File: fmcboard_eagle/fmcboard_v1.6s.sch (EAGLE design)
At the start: 300 parts, among them IC1 OPA699ID, IC10 LM358, IC11 7805DT, IC12 SN74AUC2G66DCTR, IC13 SN74AUC2G66DCTR, IC14 SN74AUC2G66DCTR, IC15 SN74AUC2G66DCTR, IC16 DAC7578SPWR, IC17 SN74AUC2G66DCTR, IC18 SN74AUC2G66DCTR, IC19 SN74AUC2G66DCTR, IC2 DAC7578SPWR, IC20 SN74AUC2G66DCTR, IC21 74AUP2GU04GW, IC22 74AUP2GU04GW, IC23 74AUP2GU04GW, IC24 74AUP2GU04GW, IC25 MC7905ACD2TR4G, IC26 AMS1117-1.8, IC27 LM358, IC28 SN74AUC2G66DCTR, IC29 LM337KVURG3, IC3 LTC6229IMS8E#TRPBF, IC30 SN74AUC2G66DCTR, IC31 SN74AUC2G66DCTR, IC32 SN74AUC2G66DCTR, IC33 LTC6229IMS8E#TRPBF, IC34 74AUP2GU04GW, IC35 74AUP2GU04GW, IC36 TPS5430DDAR, IC37 TPS5430DDAR, IC4 OPA695IDR, IC5 LTC6229IMS8E#TRPBF, IC6 OPA695IDR, IC7 OPA699ID, IC8 LM358, IC9 LM358, J1 8pin, J12 4p-2.54, J13 4p-2.54, J2 ASP-134604-01, J3 2p-2.54, J4 4p-2.54, J5 4p-2.54, J8 4p-2.54, J9 2p-2.54

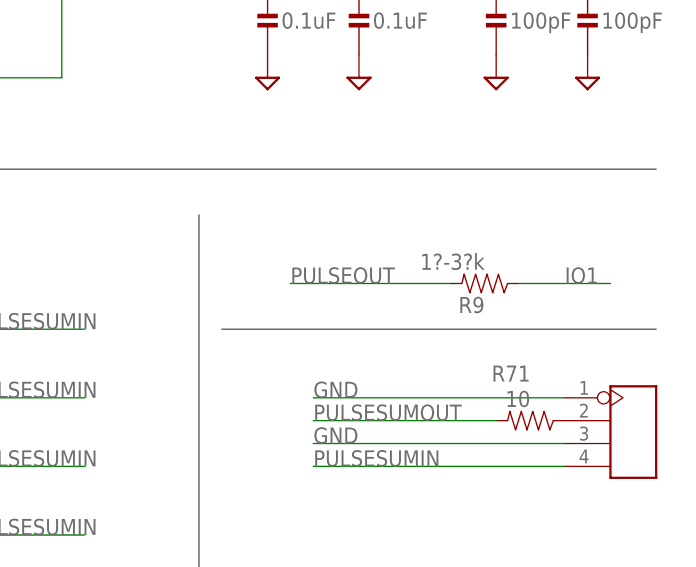
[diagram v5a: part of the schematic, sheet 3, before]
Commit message: v1.652s 0805 test resistor instead of 0402
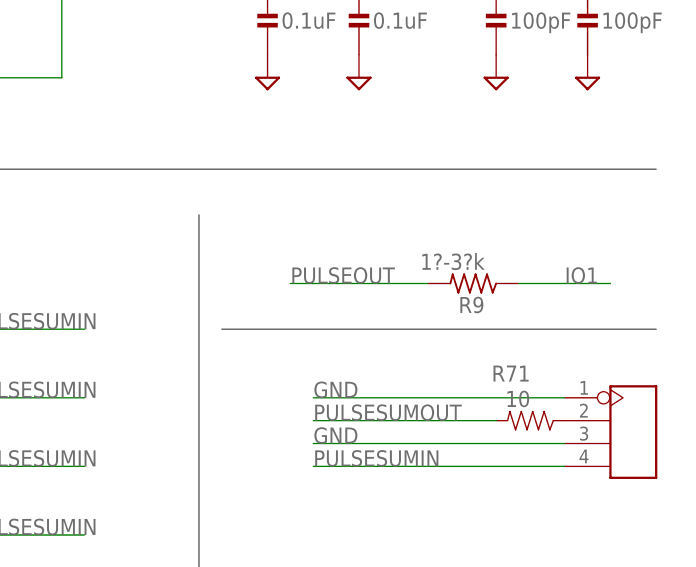
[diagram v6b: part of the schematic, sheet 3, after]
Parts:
- R9: device passives:RESISTOR0402_RES -> rcl:R-US_R0805
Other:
- moved on the sheet: R9
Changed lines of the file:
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@@
 <part name="SUPPLY125" library="supply2" library_urn="urn:adsk.eagle:library:372" deviceset="GND" device=""/>
 <part name="IC1" library="OPA699ID" deviceset="OPA699ID" device=""/>
-<part name="R9" library="passives" deviceset="RESISTOR" device="0402_RES" value="1?-3?k"/>
+<part name="R9" library="rcl" library_urn="urn:adsk.eagle:library:334" deviceset="R-US_" device="R0805" package3d_urn="urn:adsk.eagle:package:23553/2" value="1?-3?k"/>
 <part name="R10" library="passives" deviceset="RESISTOR" device="0402_RES" value="100"/>
 <part name="SUPPLY1" library="supply2" library_urn="urn:adsk.eagle:library:372" deviceset="GND" device=""/>
@@
 <segment>
 <pinref part="R9" gate="G$1" pin="2"/>
-<wire x1="269.24" y1="48.26" x2="251.46" y2="48.26" width="0.1524" layer="91"/>
+<wire x1="266.7" y1="48.26" x2="251.46" y2="48.26" width="0.1524" layer="91"/>
 <label x="251.46" y="48.26" size="1.778" layer="95"/>
 </segment>

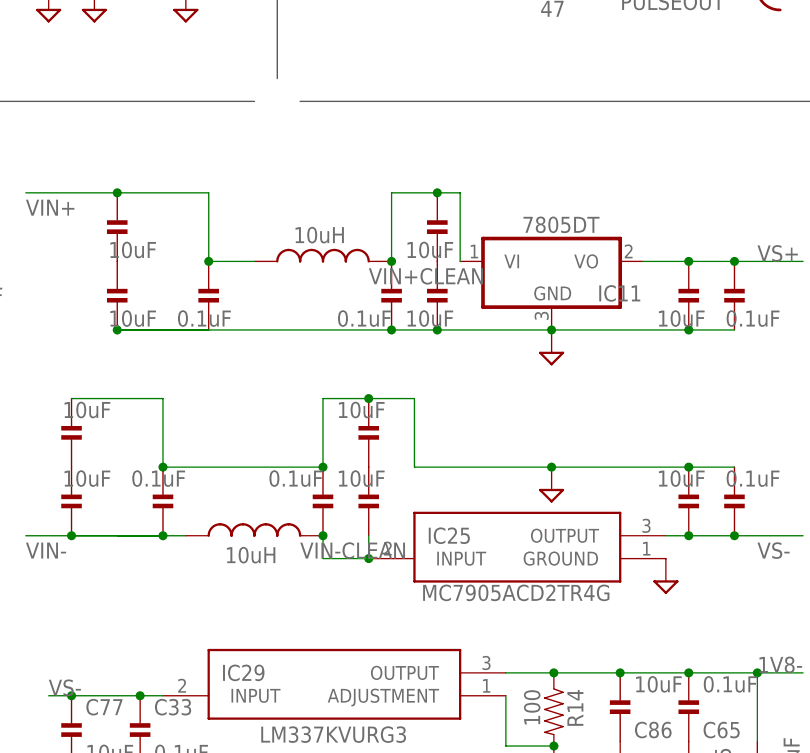
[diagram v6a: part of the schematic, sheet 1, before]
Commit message: fix VIN-
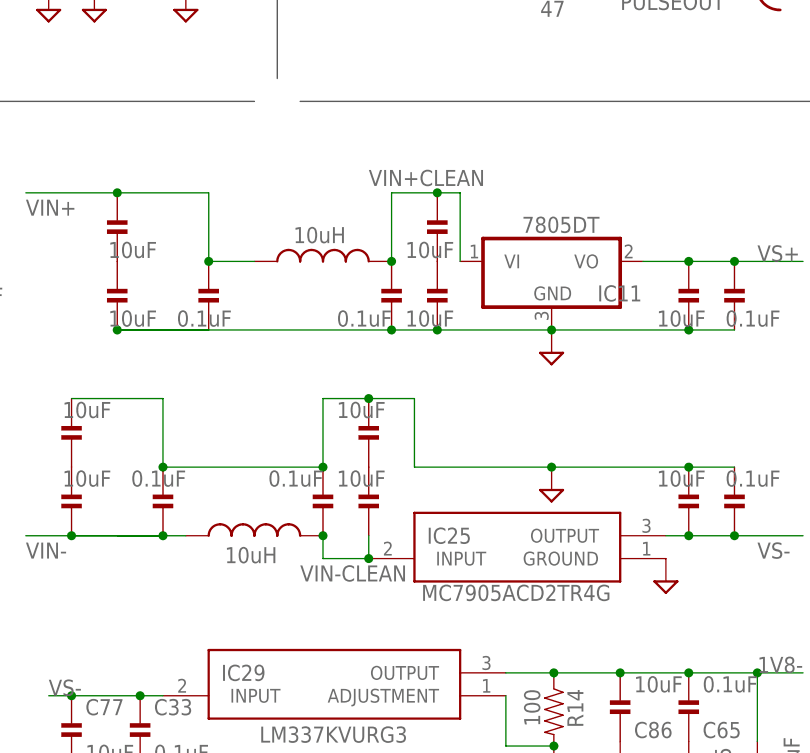
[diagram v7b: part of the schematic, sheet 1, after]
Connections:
- removed net V-: IC36.EP, IC36.GND
- net VIN-: now also IC36.EP, IC36.GND
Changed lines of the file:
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@@
 <description>Power, IO, Arduino</description>
 <plain>
-<text x="-10.16" y="48.26" size="1.778" layer="90">Linear +- power supplies and smoothing</text>
+<text x="-20.32" y="50.8" size="1.778" layer="90">Linear +- power supplies and smoothing</text>
 <text x="73.66" y="45.72" size="1.778" layer="90">Power inputs</text>
 <wire x1="111.76" y1="109.22" x2="111.76" y2="58.42" width="0.1524" layer="97"/>
@@
 AR_5V and VS+</text>
 <text x="-2.54" y="-22.86" size="1.778" layer="90">-1.25V x (1+47/100) = -1.84V</text>
-<text x="-83.82" y="48.26" size="1.778" layer="90">1.8V regulator</text>
+<text x="-71.12" y="50.8" size="1.778" layer="90">1.8V regulator</text>
 </plain>
 <instances>
@@
 <wire x1="20.32" y1="45.72" x2="25.4" y2="45.72" width="0.1524" layer="91"/>
 <pinref part="C43" gate="G$1" pin="1"/>
-<label x="17.78" y="35.56" size="1.778" layer="95"/>
+<label x="17.78" y="46.482" size="1.778" layer="95"/>
 <pinref part="C2" gate="G$1" pin="1"/>
 <junction x="25.4" y="45.72"/>
@@
 <net name="VIN-CLEAN" class="1">
 <segment>
-<label x="10.16" y="5.08" size="1.778" layer="95"/>
+<label x="10.16" y="2.54" size="1.778" layer="95"/>
 <pinref part="IC25" gate="G$1" pin="INPUT"/>
 <wire x1="12.7" y1="7.62" x2="12.7" y2="5.08" width="0.1524" layer="91"/>
@@
 </busses>
 <nets>
-<net name="V-" class="0">
-<segment>
-<wire x1="60.96" y1="-38.1" x2="53.34" y2="-38.1" width="0.1524" layer="91"/>
-<label x="55.88" y="-38.1" size="1.778" layer="95"/>
-<pinref part="IC36" gate="G$1" pin="GND"/>
-<pinref part="IC36" gate="G$1" pin="EP"/>
-<wire x1="38.1" y1="-53.34" x2="38.1" y2="-38.1" width="0.1524" layer="91"/>
-<wire x1="38.1" y1="-38.1" x2="53.34" y2="-38.1" width="0.1524" layer="91"/>
-<junction x="53.34" y="-38.1"/>
-</segment>
-</net>
 <net name="SW2" class="0">
 <segment>
@@
 <pinref part="C106" gate="G$1" pin="2"/>
 </segment>
+<segment>
+<wire x1="60.96" y1="-38.1" x2="53.34" y2="-38.1" width="0.1524" layer="91"/>
+<label x="55.88" y="-38.1" size="1.778" layer="95"/>
+<pinref part="IC36" gate="G$1" pin="GND"/>
+<pinref part="IC36" gate="G$1" pin="EP"/>
+<wire x1="38.1" y1="-53.34" x2="38.1" y2="-38.1" width="0.1524" layer="91"/>
+<wire x1="38.1" y1="-38.1" x2="53.34" y2="-38.1" width="0.1524" layer="91"/>
+<junction x="53.34" y="-38.1"/>
+</segment>
 </net>

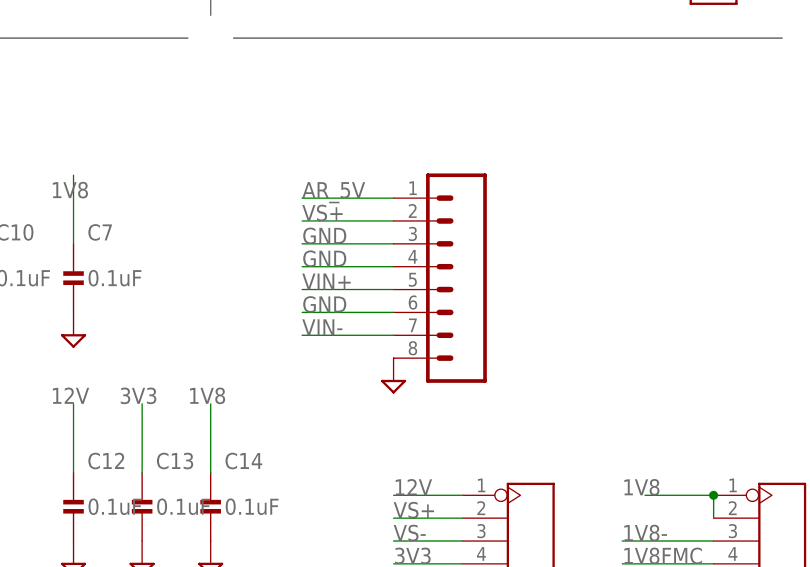
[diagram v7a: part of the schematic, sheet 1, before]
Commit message: remove pulsein hole
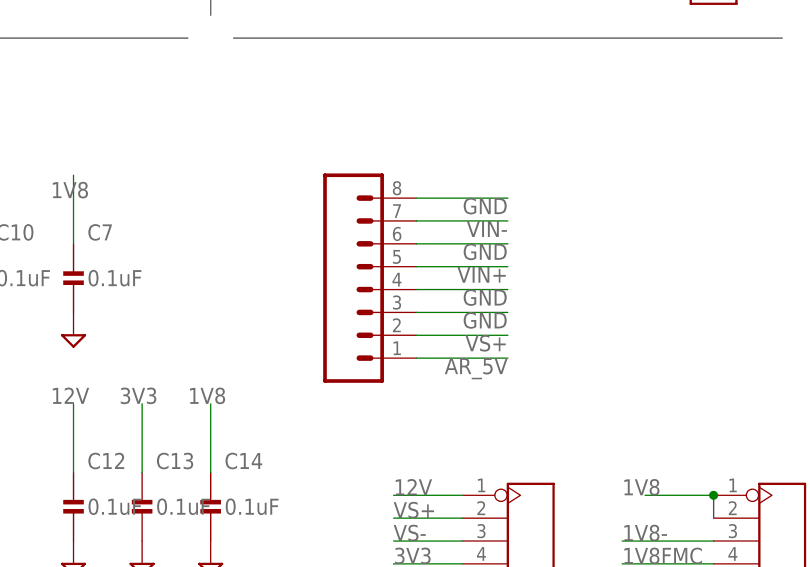
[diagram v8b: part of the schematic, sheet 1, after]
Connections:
- net GND: no longer J13.P$3
- net PULSESUMIN: no longer J13.P$4
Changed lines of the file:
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@@
 <part name="SUPPLY41" library="supply2" library_urn="urn:adsk.eagle:library:372" deviceset="GND" device=""/>
 <part name="SUPPLY43" library="supply2" library_urn="urn:adsk.eagle:library:372" deviceset="GND" device=""/>
-<part name="SUPPLY49" library="supply2" library_urn="urn:adsk.eagle:library:372" deviceset="GND" device=""/>
 <part name="C6" library="passives" deviceset="CAPACITOR" device="0402_CAP" value="0.1uF"/>
 <part name="C15" library="passives" deviceset="CAPACITOR" device="0402_CAP" value="0.1uF"/>
@@
 <instances>
 <instance part="J12" gate="G$1" x="175.26" y="1.27" smashed="yes"/>
-<instance part="J1" gate="G$1" x="137.16" y="30.48" smashed="yes" rot="R180"/>
+<instance part="J1" gate="G$1" x="129.54" y="27.94" smashed="yes"/>
 <instance part="C3" gate="G$1" x="-2.54" y="73.66" smashed="yes">
 <attribute name="NAME" x="-1.016" y="76.581" size="1.778" layer="95"/>
@@
 </instance>
 <instance part="SUPPLY41" gate="GND" x="66.04" y="68.58" smashed="yes"/>
-<instance part="SUPPLY49" gate="GND" x="132.08" y="17.78" smashed="yes"/>
 <instance part="R34" gate="G$1" x="40.64" y="68.58" smashed="yes">
 <attribute name="NAME" x="36.83" y="70.0786" size="1.778" layer="95"/>
@@
 </segment>
 <segment>
-<pinref part="J1" gate="G$1" pin="8"/>
-<pinref part="SUPPLY49" gate="GND" pin="GND"/>
-</segment>
-<segment>
 <pinref part="SUPPLY31" gate="GND" pin="GND"/>
 <junction x="38.1" y="30.48"/>
@@
 <segment>
 <pinref part="J1" gate="G$1" pin="6"/>
-<wire x1="121.92" y1="25.4" x2="132.08" y2="25.4" width="0.1524" layer="91"/>
-<label x="121.92" y="25.4" size="1.778" layer="95"/>
+<wire x1="144.78" y1="33.02" x2="134.62" y2="33.02" width="0.1524" layer="91"/>
+<label x="144.78" y="33.02" size="1.778" layer="95" rot="R180"/>
 </segment>
 <segment>
@@
 </segment>
 <segment>
-<wire x1="121.92" y1="30.48" x2="132.08" y2="30.48" width="0.1524" layer="91"/>
+<wire x1="144.78" y1="27.94" x2="134.62" y2="27.94" width="0.1524" layer="91"/>
 <pinref part="J1" gate="G$1" pin="4"/>
-<label x="121.92" y="30.48" size="1.778" layer="95"/>
+<label x="144.78" y="27.94" size="1.778" layer="95" rot="R180"/>
 </segment>
 <segment>
-<wire x1="121.92" y1="33.02" x2="132.08" y2="33.02" width="0.1524" layer="91"/>
+<wire x1="144.78" y1="25.4" x2="134.62" y2="25.4" width="0.1524" layer="91"/>
 <pinref part="J1" gate="G$1" pin="3"/>
-<label x="121.92" y="33.02" size="1.778" layer="95"/>
+<label x="144.78" y="25.4" size="1.778" layer="95" rot="R180"/>
 </segment>
 <segment>
@@
 <pinref part="SUPPLY125" gate="GND" pin="GND"/>
 </segment>
+<segment>
+<pinref part="J1" gate="G$1" pin="8"/>
+<wire x1="134.62" y1="38.1" x2="144.78" y2="38.1" width="0.1524" layer="91"/>
+<label x="144.78" y="38.1" size="1.778" layer="95" rot="R180"/>
+</segment>
 </net>
 <net name="1V8" class="1">
@@
 <segment>
 <pinref part="J1" gate="G$1" pin="2"/>
-<wire x1="132.08" y1="35.56" x2="121.92" y2="35.56" width="0.1524" layer="91"/>
-<label x="121.92" y="35.56" size="1.778" layer="95"/>
+<wire x1="134.62" y1="22.86" x2="144.78" y2="22.86" width="0.1524" layer="91"/>
+<label x="144.78" y="22.86" size="1.778" layer="95" rot="R180"/>
 </segment>
 <segment>
@@
 <segment>
 <pinref part="J1" gate="G$1" pin="1"/>
-<wire x1="132.08" y1="38.1" x2="121.92" y2="38.1" width="0.1524" layer="91"/>
-<label x="121.92" y="38.1" size="1.778" layer="95"/>
+<wire x1="134.62" y1="20.32" x2="144.78" y2="20.32" width="0.1524" layer="91"/>
+<label x="144.78" y="20.32" size="1.778" layer="95" rot="R180"/>
 </segment>
 <segment>
@@
 <segment>
 <pinref part="J1" gate="G$1" pin="5"/>
-<wire x1="121.92" y1="27.94" x2="132.08" y2="27.94" width="0.1524" layer="91"/>
-<label x="121.92" y="27.94" size="1.778" layer="95"/>
+<wire x1="144.78" y1="30.48" x2="134.62" y2="30.48" width="0.1524" layer="91"/>
+<label x="144.78" y="30.48" size="1.778" layer="95" rot="R180"/>
 </segment>
 <segment>
@@
 <segment>
 <pinref part="J1" gate="G$1" pin="7"/>
-<wire x1="132.08" y1="22.86" x2="121.92" y2="22.86" width="0.1524" layer="91"/>
-<label x="121.92" y="22.86" size="1.778" layer="95"/>
+<wire x1="134.62" y1="35.56" x2="144.78" y2="35.56" width="0.1524" layer="91"/>
+<label x="144.78" y="35.56" size="1.778" layer="95" rot="R180"/>
 </segment>
 </net>
@@
 </segment>
 <segment>
-<wire x1="281.94" y1="30.48" x2="254" y2="30.48" width="0.1524" layer="91"/>
-<label x="254" y="30.48" size="1.778" layer="95"/>
-<pinref part="J13" gate="G$1" pin="P$3"/>
-</segment>
-<segment>
 <label x="256.54" y="2.54" size="1.778" layer="95"/>
 <wire x1="256.54" y1="2.54" x2="281.94" y2="2.54" width="0.1524" layer="91"/>
@@
 <label x="215.9" y="-10.16" size="1.778" layer="95"/>
 </segment>
-<segment>
-<pinref part="J13" gate="G$1" pin="P$4"/>
-<wire x1="281.94" y1="27.94" x2="256.54" y2="27.94" width="0.1524" layer="91"/>
-<wire x1="254" y1="27.94" x2="256.54" y2="27.94" width="0.1524" layer="91"/>
-<label x="254" y="27.94" size="1.778" layer="95"/>
-</segment>
 </net>
